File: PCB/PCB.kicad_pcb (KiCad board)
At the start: 2 copper layers, 31 parts, among them Q101 BC817, Q102 BC817, Q103 BC817, Q104 BC817, Q301 BC807, Q302 BC807, Q401 DMP3125L, U101 TSV782, U102 OJ-SH-105HM, U103 OJ-SH-105HM, U104 OJ-SH-105HM, U105 OJ-SH-105HM, U203 74HC193, U204 74HC139, U301 TLV3542, U303 LM321, U401 LDK320, U402 LMR54410DBVR, U403 TLV3542, U404 NCP431

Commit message: changes
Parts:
- removed U204: 74HC139, w-ic:SOIC-16 3.9x9.9mm P1.27mm
- removed U303: LM321, w-ic:SOT-23-5L
- added C101: 2u2, Capacitor_SMD:C_0603_1608Metric, F.Cu at (73.3, 66.5)
- added C102: 100n, Capacitor_SMD:C_0603_1608Metric, F.Cu at (73.3, 69.0)
- added C201: 100n, Capacitor_SMD:C_0603_1608Metric, F.Cu at (110.7, 80.6)
- added C202: 100n, Capacitor_SMD:C_0603_1608Metric, F.Cu at (110.7, 83.1)
- added C203: 100n, Capacitor_SMD:C_0603_1608Metric, F.Cu at (110.7, 85.7)
- added C204: 100n, Capacitor_SMD:C_0603_1608Metric, F.Cu at (110.7, 88.2)
- added C205: 100n, Capacitor_SMD:C_0603_1608Metric, F.Cu at (110.7, 90.7)
- added C206: 100n, Capacitor_SMD:C_0603_1608Metric, F.Cu at (110.7, 93.2)
- added C301: 100n, Capacitor_SMD:C_0603_1608Metric, F.Cu at (49.5, 95.1)
- added C302: 2u2, Capacitor_SMD:C_0603_1608Metric, F.Cu at (80.2, 106.0)
- added C303: 2u2, Capacitor_SMD:C_0603_1608Metric, F.Cu at (80.2, 108.5)
- added C304: 100n, Capacitor_SMD:C_0603_1608Metric, F.Cu at (49.5, 102.6)
- added C305: 100n, Capacitor_SMD:C_0603_1608Metric, F.Cu at (49.5, 105.1)
- added C401: 1u, Capacitor_SMD:C_0603_1608Metric, F.Cu at (111.9, 63.6)
- added C402: 100u, Capacitor_THT:C_Radial_D6.3mm_H11.0mm_P2.50mm, F.Cu at (112.6, 50.5)
- added C403: 1u, Capacitor_SMD:C_0603_1608Metric, F.Cu at (111.9, 66.1)
- added C404: 100n, Capacitor_SMD:C_0603_1608Metric, F.Cu at (111.9, 68.6)
- added C405: 100u, Capacitor_THT:C_Radial_D6.3mm_H11.0mm_P2.50mm, F.Cu at (112.6, 58.4)
- added C409: 100n, Capacitor_SMD:C_0603_1608Metric, F.Cu at (115.9, 63.6)
- added C411: 100n, Capacitor_SMD:C_0603_1608Metric, F.Cu at (115.9, 68.6)
- added C412: 100n, Capacitor_SMD:C_0603_1608Metric, F.Cu at (115.9, 71.1)
- added D201: LED_R, LED_SMD:LED_0603_1608Metric, F.Cu at (110.7, 95.7)
- added D202: LED_R, LED_SMD:LED_0603_1608Metric, F.Cu at (110.7, 98.3)
- added D203: LED_R, LED_SMD:LED_0603_1608Metric, F.Cu at (110.7, 100.9)
- added D204: LED_R, LED_SMD:LED_0603_1608Metric, F.Cu at (110.7, 103.5)
- added D301: SS24, w-diode:SOD-123LF, F.Cu at (85.0, 106.2)
- added D302: SS24, w-diode:SOD-123LF, F.Cu at (85.0, 109.3)
- added D303: LED_R, LED_SMD:LED_0603_1608Metric, F.Cu at (67.2, 104.0)
- added D401: LED_G, LED_SMD:LED_0603_1608Metric, F.Cu at (119.8, 56.1)
- added J101: Current_input, TerminalBlock_Phoenix:TerminalBlock_Phoenix_MPT-0,5-2-2.54_1x02_P2.54mm_Horizontal, F.Cu at (81.9, 81.6)
- added J102: Banana conn. red, w-connector:J.40024.2, F.Cu at (76.5, 59.7)
- added J103: Banana conn. black, w-connector:J.40024.2, F.Cu at (76.5, 63.4)
- added J104: Conn_Coaxial, w-connector:GOLDEN LOCH 900D-6452R2, F.Cu at (72.4, 52.2)
- added J401: Barrel_Jack_Switch, w-connector:Barrel jack 6,4mm, F.Cu at (103.1, 55.0)
- added L401: 68u, w-magnetics:Shielded L 6x6x4.2mm, F.Cu at (101.1, 67.1)
- added R101: 4k7, Resistor_SMD:R_0603_1608Metric, F.Cu at (73.3, 71.5)
- added R102: 4k7, Resistor_SMD:R_0603_1608Metric, F.Cu at (73.3, 74.0)
- added R103: 4k7, Resistor_SMD:R_0603_1608Metric, F.Cu at (73.3, 76.5)
- added R104: 4k7, Resistor_SMD:R_0603_1608Metric, F.Cu at (73.3, 79.0)
- added R105: 100R, Resistor_SMD:R_0603_1608Metric, F.Cu at (77.3, 66.5)
- added R106: 1k, Resistor_SMD:R_0603_1608Metric, F.Cu at (77.3, 69.0)
- added R107: 100k, Resistor_SMD:R_0603_1608Metric, F.Cu at (77.3, 71.5)
- added R108: 10M, Resistor_SMD:R_1206_3216Metric, F.Cu at (89.7, 85.3)
- added R109: 51R, Resistor_SMD:R_0603_1608Metric, F.Cu at (77.3, 74.0)
- added R110: 100k, Resistor_SMD:R_0603_1608Metric, F.Cu at (77.3, 76.5)
- added R201: 10k, Resistor_SMD:R_0603_1608Metric, F.Cu at (114.7, 80.6)
- added R202: 10k, Resistor_SMD:R_0603_1608Metric, F.Cu at (114.7, 83.1)
- added R203: 10k, Resistor_SMD:R_0603_1608Metric, F.Cu at (114.7, 85.7)
- added R204: 10k, Resistor_SMD:R_0603_1608Metric, F.Cu at (114.7, 88.2)
- added R205: 10k, Resistor_SMD:R_0603_1608Metric, F.Cu at (114.7, 90.7)
- added R206: 1k, Resistor_SMD:R_0603_1608Metric, F.Cu at (114.7, 93.2)
- added R207: 1k, Resistor_SMD:R_0603_1608Metric, F.Cu at (118.7, 80.6)
- added R208: 1k, Resistor_SMD:R_0603_1608Metric, F.Cu at (118.7, 83.1)
- added R209: 1k, Resistor_SMD:R_0603_1608Metric, F.Cu at (118.7, 85.7)
- added R301: 100k, Resistor_SMD:R_0603_1608Metric, F.Cu at (49.5, 107.6)
- added R302: 100k, Resistor_SMD:R_0603_1608Metric, F.Cu at (49.5, 110.1)
- added R303: 51k, Resistor_SMD:R_0603_1608Metric, F.Cu at (53.5, 95.1)
- added R304: 51k, Resistor_SMD:R_0603_1608Metric, F.Cu at (53.5, 97.6)
- added R305: 100k, Resistor_SMD:R_0603_1608Metric, F.Cu at (53.5, 100.1)
- added R306: 100k, Resistor_SMD:R_0603_1608Metric, F.Cu at (53.5, 102.6)
- added R307: 1M, Resistor_SMD:R_0603_1608Metric, F.Cu at (80.2, 111.0)
- added R308: 1M, Resistor_SMD:R_0603_1608Metric, F.Cu at (80.2, 113.5)
- added R309: 1k, Resistor_SMD:R_0603_1608Metric, F.Cu at (53.5, 110.1)
- added R310: 100k, Resistor_SMD:R_0603_1608Metric, F.Cu at (57.5, 95.1)
- added R311: 100k, Resistor_SMD:R_0603_1608Metric, F.Cu at (57.5, 97.6)
- added R312: 100k, Resistor_SMD:R_0603_1608Metric, F.Cu at (57.5, 100.1)
- added R313: 270R, Resistor_SMD:R_0603_1608Metric, F.Cu at (57.5, 102.6)
- added R401: 1k, Resistor_SMD:R_0603_1608Metric, F.Cu at (115.9, 76.1)
- added R404: 22k, Resistor_SMD:R_0603_1608Metric, F.Cu at (119.9, 68.6)
- added SW101: SW_Push, Connector_PinHeader_2.54mm:PinHeader_1x02_P2.54mm_Vertical, F.Cu at (87.3, 67.5)
- added SW102: SW_Push, Connector_PinHeader_2.54mm:PinHeader_1x02_P2.54mm_Vertical, F.Cu at (91.9, 67.5)
- added U106: 74HC00, w-ic:SOIC-14 3.9x8.6mm P1.27mm, F.Cu at (102.5, 100.5)
- added U201: 74HC193, w-ic:SOIC-16 3.9x9.9mm P1.27mm, F.Cu at (103.1, 83.6)
- added U202: 74HC139, w-ic:SOIC-16 3.9x9.9mm P1.27mm, F.Cu at (103.1, 92.0)
- added U302: LM321, w-ic:SOT-23-5L, F.Cu at (67.2, 99.9)
- D101, D102, D103, D104: footprint Diode_SMD:D_SMA -> w-diode:SOD-123LF
- Q301, Q302: value BC807 -> DMP3125L; footprint w-ic:SOT-23 -> w-transistor:SOT23-3
- R402: value 118k -> 4k7
- R403: value 22k -> 118k
- U203: value 74HC193 -> 74HC14; footprint w-ic:SOIC-16 3.9x9.9mm P1.27mm -> w-ic:SOIC-14 3.9x8.6mm P1.27mm
- U301: value TLV3542 -> LM321; footprint w-ic:SOIC-8 -> w-ic:SOT-23-5L
- U403: value TLV3542 -> NCP431; footprint w-ic:SOIC-8 -> w-ic:SOT-23
- U404: value NCP431 -> TLV9361xDBV; footprint w-ic:SOT-23 -> w-ic:SOT-23-5L
- moved R402 40.6 mm to (119.9, 63.6)
- moved R403 40.6 mm to (119.9, 66.1)
- moved C406 40.5 mm to (111.9, 71.1)
- moved C407 40.5 mm to (111.9, 73.6)
- moved C408 40.5 mm to (111.9, 76.1)
- moved FB401 40.1 mm to (115.9, 73.6)
- moved U301 39.0 mm to (67.2, 95.8)
- moved Q302 38.3 mm to (62.2, 100.5)
- moved C410 38.2 mm to (115.9, 66.1)
- moved Q301 38.1 mm to (62.2, 96.0)
- moved U403 34.6 mm to (120.1, 52.7)
- moved U404 30.6 mm to (120.1, 48.6)
- moved U203 29.8 mm to (92.2, 97.8)
- moved Q401 25.7 mm to (106.4, 73.1)
- moved U401 24.9 mm to (100.7, 73.9)
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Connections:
- C406 pad 2: GND2 -> GND
- C407 pad 2: GND2 -> GND
- C408 pad 1: Net-(U402-CB) -> +5VA
- C408 pad 2: Net-(U402-SW) -> GND
- C410 pad 1: GND2 -> GND
- Q301 pad 1: Net-(Q301-B) -> /overrange_detecor/+OR
- Q301 pad 2: Net-(Q301-E) -> GNDA
- Q301 pad 3: GNDA -> Net-(Q301-S)
- Q302 pad 1: Net-(Q302-B) -> /overrange_detecor/-OR
- Q302 pad 2: Net-(Q302-E) -> GNDA
- Q302 pad 3: GNDA -> Net-(Q301-S)
- R402 pad 1: Net-(U402-FB) -> +5VA
- R402 pad 2: +5V -> Net-(U403-K)
- R403 pad 1: GND2 -> Net-(U402-FB)
- R403 pad 2: Net-(U402-FB) -> +5V
- U203 pad 1: GND -> Net-(C202-Pad1)
- U203 pad 10: GND -> /range_selector/R3
- U203 pad 12: unconnected-(U203-~{CO}-Pad12) -> /range_selector/R4
- U203 pad 13: unconnected-(U203-~{BO}-Pad13) -> Net-(U202-~{1Y3})
- U203 pad 14: GND -> +5V
- U203 pad 2: /range_selector/CT_MSB -> Net-(U106-Pad1)
- U203 pad 3: /range_selector/CT_LSB -> Net-(C203-Pad1)
- U203 pad 4: /range_selector/CT_DOWN -> Net-(U106-Pad5)
- U203 pad 5: /range_selector/CT_UP -> Net-(U202-~{1Y0})
- U203 pad 6: unconnected-(U203-QC-Pad6) -> /range_selector/R1
- U203 pad 7: unconnected-(U203-QD-Pad7) -> GND
- U203 pad 8: GND -> /range_selector/R2
- U203 pad 9: GND -> Net-(U202-~{1Y1})
- U301 pad 1: (no net) -> GNDA
- U301 pad 2: (no net) -> +5VA
- U301 pad 3: (no net) -> Net-(U301--)
- U301 pad 4: (no net) -> Net-(R302-Pad2)
- U301 pad 5: GNDA -> GND
- U401 pad 2: Net-(U401-GND) -> GND
- U402 pad 2: GND2 -> GND
- U403 pad 1: GNDA -> Net-(U403-K)
- U403 pad 2: GNDA -> Net-(U403-K)
- U403 pad 3: Net-(U403A-+) -> GND
- U404 pad 1: Net-(U403A-+) -> GNDA
- U404 pad 2: Net-(U403A-+) -> GND
- U404 pad 3: GND -> GNDA

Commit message: start of layout
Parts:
- removed R205: 10k, Resistor_SMD:R_0603_1608Metric
- removed U403: NCP431, w-ic:SOT-23
- added R405: 100k, Resistor_SMD:R_0603_1608Metric, F.Cu at (234.6, 75.2)
- C410: footprint Capacitor_SMD:C_0603_1608Metric -> Capacitor_SMD:C_0805_2012Metric
- D201, D202, D203, D204, D303: footprint LED_SMD:LED_0603_1608Metric -> LED_THT:LED_D3.0mm
- D401: footprint LED_SMD:LED_0603_1608Metric -> LED_THT:LED_D3.0mm_Clear
- R401: value 1k -> 4k7
- R402: value 4k7 -> 100k
- moved J104 184.6 mm to (250.6, 100.1)
- moved J103 177.2 mm to (251.9, 88.7)
- moved J102 176.3 mm to (251.8, 78.5)
- moved C305 174.5 mm to (223.9, 100.5)
- moved R109 165.7 mm to (241.0, 100.0)
- moved R311 164.7 mm to (222.0, 106.6), turned to 90 degrees
- moved C304 161.3 mm to (210.7, 108.5)
- moved D303 158.4 mm to (225.5, 109.6)
- moved R310 158.4 mm to (215.8, 100.7)
- moved R312 158.4 mm to (215.8, 105.7)
- moved R313 158.4 mm to (215.8, 108.2)
- moved U302 156.6 mm to (223.8, 102.8)
- moved J401 151.9 mm to (255.0, 54.0), turned to 90 degrees
- moved Q401 138.1 mm to (242.7, 51.0)
- moved U401 133.7 mm to (234.0, 64.4), turned to 180 degrees
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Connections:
- net Net-(D303-K) renamed /overrange_detecor/OR_OUT
- U102 pad 1: (no net) -> +5V
- U102 pad 2: +5V -> Net-(D101-A)
- U103 pad 1: (no net) -> +5V
- U103 pad 2: +5V -> Net-(D102-A)
- U104 pad 1: (no net) -> +5V
- U104 pad 2: +5V -> Net-(D103-A)
- U105 pad 1: (no net) -> +5V
- U105 pad 2: +5V -> Net-(D104-A)
- U106 pad 2: /range_selector/R4 -> Net-(U202-~{1Y3})
- U106 pad 4: /range_selector/R1 -> Net-(U202-~{1Y0})
- U201 pad 11: Net-(U201-~{LOAD}) -> +5V
- U202 pad 15: GND -> +5V

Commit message: rough layout done
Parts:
- added REF**: MountingHole_3.2mm_M3, MountingHole:MountingHole_3.2mm_M3, F.Cu at (127.5, 68.5)
- added REF**: MountingHole_3.2mm_M3, MountingHole:MountingHole_3.2mm_M3, F.Cu at (127.5, 119.5)
- added REF**: MountingHole_3.2mm_M3, MountingHole:MountingHole_3.2mm_M3, F.Cu at (218.5, 81.4)
- J101: footprint TerminalBlock_Phoenix:TerminalBlock_Phoenix_MPT-0,5-2-2.54_1x02_P2.54mm_Horizontal -> w-connector:Terminal Block 2x3,5mm
- SW101, SW102: footprint Connector_PinHeader_2.54mm:PinHeader_1x02_P2.54mm_Vertical -> Button_Switch_THT:SW_Tactile_SPST_Angled_PTS645Vx83-2LFS
- moved C101 136.7 mm to (203.7, 107.6), turned to 180 degrees
- moved R110 130.5 mm to (203.7, 109.1)
- moved R309 116.8 mm to (192.7, 90.2), turned to 90 degrees
- moved Q301 98.7 mm to (190.8, 100.5), turned to 90 degrees
- moved Q302 96.6 mm to (187.3, 100.6), turned to 90 degrees
- moved R306 90.7 mm to (173.5, 106.0), turned to 90 degrees
- moved R405 89.6 mm to (154.0, 114.4), turned to 180 degrees
- moved C408 89.5 mm to (151.7, 118.5)
- moved C411 89.5 mm to (151.0, 121.1)
- moved C412 89.5 mm to (154.0, 121.1)
- moved R402 89.5 mm to (154.0, 115.9)
- moved U404 89.5 mm to (154.0, 118.5)
- moved R304 88.0 mm to (172.0, 106.0), turned to 90 degrees
- moved R305 87.2 mm to (170.5, 106.0), turned to 90 degrees
- moved R303 84.6 mm to (169.0, 106.0), turned to 90 degrees
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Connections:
- U302 pad 2: +5V -> GND
- U302 pad 5: GND -> +5V
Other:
- board outline added: 100 x 60 mm

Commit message: almost done
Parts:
- C404, FB401: moved to B.Cu
- moved C403 36.6 mm to (205.9, 82.0)
- moved C401 36.6 mm to (205.9, 79.2)
- moved U401 36.6 mm to (202.5, 80.6)
- moved D303 13.4 mm to (193.2, 80.6), turned to 180 degrees
- moved R306 8.20 mm to (171.9, 114.1)
- moved R304 8.20 mm to (173.4, 114.1)
- moved R303 8.05 mm to (168.9, 114.1)
- moved R305 8.05 mm to (170.4, 114.1)
- moved R312 7.18 mm to (194.6, 91.2)
- moved C305 7.18 mm to (192.3, 95.7)
- moved R309 7.18 mm to (190.0, 96.8)
- moved R310 7.18 mm to (192.3, 90.4)
- moved C304 7.18 mm to (190.0, 90.8)
- moved R311 7.18 mm to (190.0, 93.8)
- moved U302 7.18 mm to (192.3, 93.1)
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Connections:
- D303 pad 1: /overrange_detecor/OR_OUT -> Net-(D303-K)
- D303 pad 2: Net-(D303-A) -> +5V
- R313 pad 1: Net-(D303-A) -> /overrange_detecor/OR_OUT
- R313 pad 2: +5V -> Net-(D303-K)
- U301 pad 2: +5VA -> GND
- U301 pad 5: GND -> +5VA
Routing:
- net +5V: track 0.00 -> 212.2 mm, vias 0 -> 7
- net GNDA: track 0.00 -> 176.6 mm, vias 0 -> 4
- net +5VA: track 0.00 -> 85.7 mm, vias 0 -> 3
- net Net-(U101B-+): track 0.00 -> 79.5 mm
- net /overrange_detecor/IN: track 0.00 -> 74.6 mm
- net /CURR_OUT: track 0.00 -> 60.3 mm
- net Net-(R105-Pad1): track 0.00 -> 48.5 mm
- net Net-(R106-Pad1): track 0.00 -> 36.9 mm
- net +12V: track 0.00 -> 34.6 mm
- net /range_selector/R1: track 0.00 -> 29.6 mm, vias 0 -> 1
- net /range_selector/RNG-: track 0.00 -> 29.3 mm, vias 0 -> 2
- net Net-(R304-Pad2): track 0.00 -> 29.2 mm
- net /range_selector/RNG+: track 0.00 -> 29.1 mm, vias 0 -> 2
- net Net-(U202-~{1Y3}): track 0.00 -> 27.8 mm, vias 0 -> 3
- net Net-(R107-Pad1): track 0.00 -> 25.3 mm
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- added copper zone on F.Cu, net +5V
- added copper zone on F.Cu, net +5VA
- added copper zone on B.Cu, net GND
- added copper zone on F.Cu, net GND
- added copper zone on B.Cu, net GNDA
- added copper zone on F.Cu, net GNDA
- added copper zone on F.Cu, net Net-(R302-Pad2)
- added copper zone on F.Cu, net Net-(U301--)
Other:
- outline, holes or cut-outs redrawn

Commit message: rev 1 done
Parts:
- added G***: LOGO, LOGO, F.Cu at (182.8, 108.2)
- added REF**: MountingHole_3.2mm_M3_DIN965, MountingHole:MountingHole_3.2mm_M3_DIN965, F.Cu at (201.5, 119.5)
- moved SW101 3.80 mm to (186.7, 121.0)
- moved C401 3.57 mm to (202.3, 79.1), turned to 180 degrees
- moved C403 1.83 mm to (206.2, 83.8)
- moved U401 1.83 mm to (202.9, 82.4)
- moved R401 1.82 mm to (206.2, 80.8)
- moved D303 1.10 mm to (193.2, 81.7)
- moved D401 1.10 mm to (212.6, 81.6)
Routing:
- net /range_selector/RNG+: track 29.1 -> 32.8 mm
- net GNDA: track 176.6 -> 180.1 mm
- net /CURR_OUT: track 60.3 -> 58.6 mm
- net +5VA: track 85.7 -> 84.1 mm
- net Net-(D401-A): track 2.37 -> 3.84 mm
- net Net-(D303-K): track 6.97 -> 5.87 mm
- net +5V: track 212.2 -> 213.2 mm
- net Net-(U106-Pad1): track 16.0 -> 16.8 mm
- net +12V: track 34.6 -> 35.1 mm
- net GND: vias 75 -> 163
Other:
- board text added: "+"
- board text added: "-"
- board text added: "100nA/V"
- board text added: "10mA/V"
- board text added: "10uA/V"
- board text added: "1mA/V"
- board text added: "6~12V"
- board text added: "I"
- board text added: "Range+"
- board text added: "Range-"

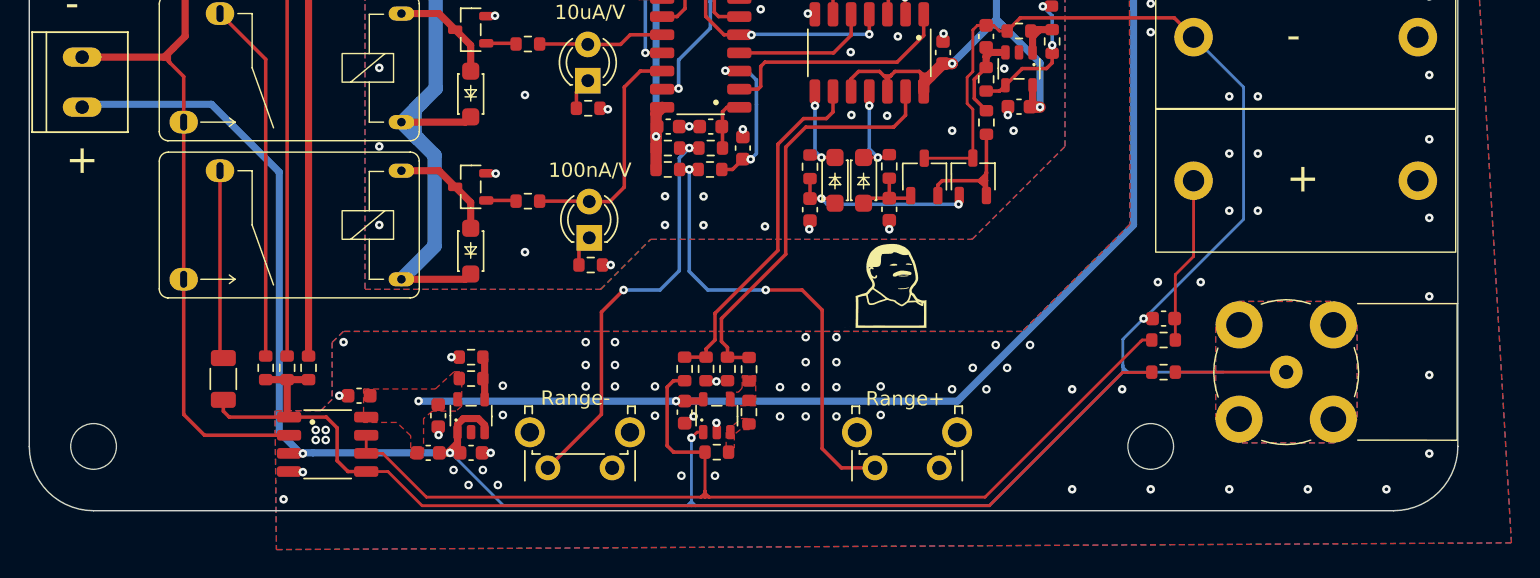
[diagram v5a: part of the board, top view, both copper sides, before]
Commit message: changed BNC footprint
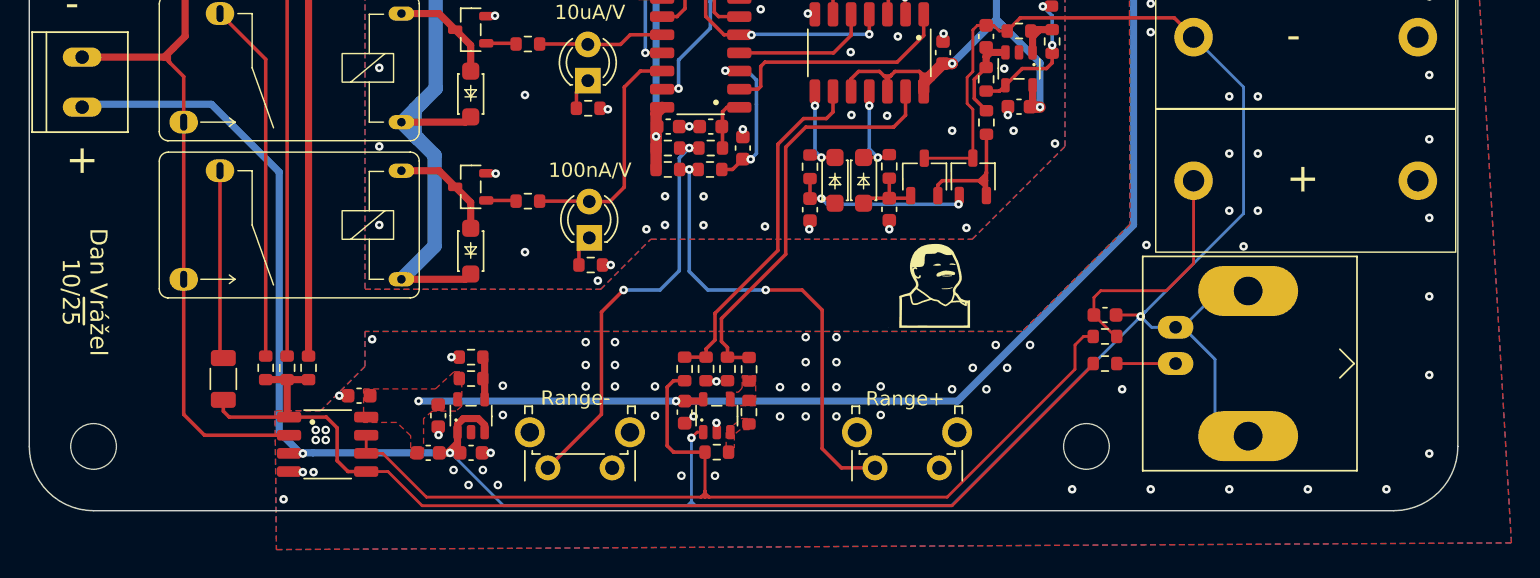
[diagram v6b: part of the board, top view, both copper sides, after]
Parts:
- J104: footprint w-connector:GOLDEN LOCH 900D-6452R2 -> Connector_Coaxial:BNC_Amphenol_B6252HB-NPP3G-50_Horizontal
- moved J104 7.77 mm to (203.2, 113.7), turned to -90 degrees
- moved REF** 4.50 mm to (197.0, 119.5)
- moved R109 4.14 mm to (198.3, 113.7)
- moved C101 4.11 mm to (198.3, 110.3), turned to 0 degrees
- moved R110 4.11 mm to (198.3, 111.8)
- moved G*** 3.05 mm to (185.9, 108.2)
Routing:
- net GNDA: track 180.1 -> 192.6 mm
- net Net-(J102-Pin_1): track 11.7 -> 17.2 mm
- net Net-(U101B-+): track 79.5 -> 75.6 mm
- net Net-(J104-In): track 7.76 -> 4.12 mm
- net /overrange_detecor/IN: track 74.6 -> 71.6 mm
- net GND: vias 163 -> 167
- removed copper zone on B.Cu, net GNDA
- removed copper zone on F.Cu, net GNDA
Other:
- board text added: "Dan Vrážel 10/~{25}"
